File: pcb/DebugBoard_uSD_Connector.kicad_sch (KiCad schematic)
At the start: 10 parts, among them J5 0472192001

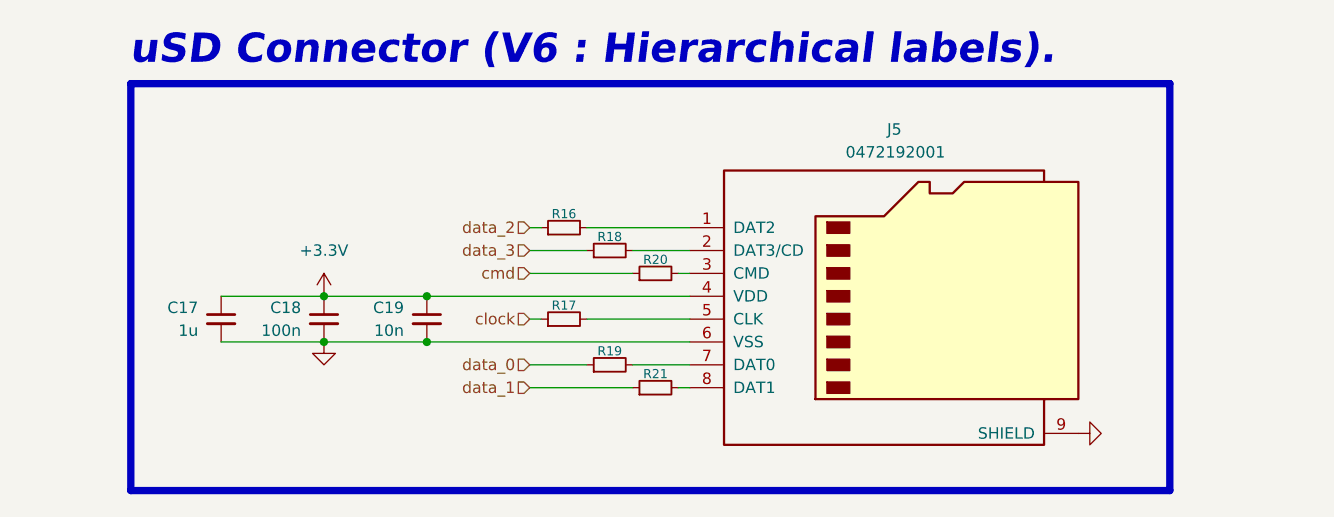
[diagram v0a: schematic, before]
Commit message: Updated uSD connector for `DebugBoard`.
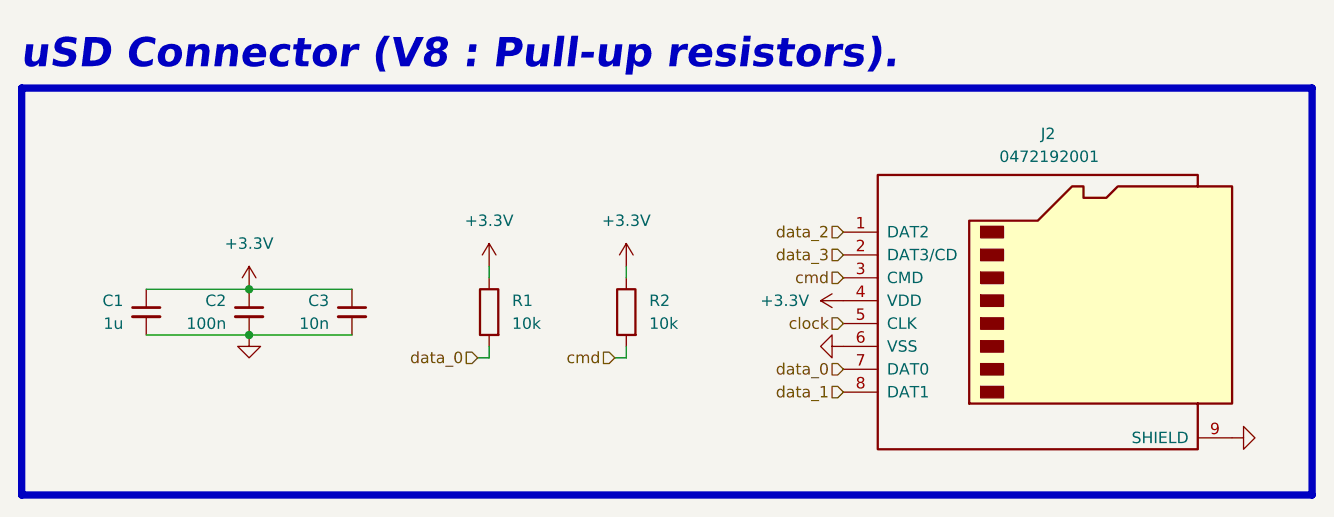
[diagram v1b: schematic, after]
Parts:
- removed R16, R17, R18, R19, R20, R21: R_Small, Resistor_SMD:R_1206_3216Metric_Pad1.30x1.75mm_HandSolder, symbol Device:R_Small
- added R1, R2: 10k, Resistor_SMD:R_1206_3216Metric_Pad1.30x1.75mm_HandSolder, symbol Device:R
- renumbered C17 to C1, C18 to C2, C19 to C3, J5 to J2
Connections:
- net +3.3V: now also R1.1, R2.1
- net clock: now also J2.5 (CLK)
- net cmd: now also J2.3 (CMD), R2.2
- net data_0: now also J2.7 (DAT0), R1.2
- net data_1: now also J2.8 (DAT1)
- net data_2: now also J2.1 (DAT2)
- net data_3: now also J2.2 (DAT3/CD)
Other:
- note added: "uSD Connector (V8 : Pull-up resistors)."
- note removed: "uSD Connector (V6 : Hierarchical labels)."
- moved on the sheet: C1, C2, C3, J2

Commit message: Made `DebugBoard` target and fixed some GPIO discrepancies.
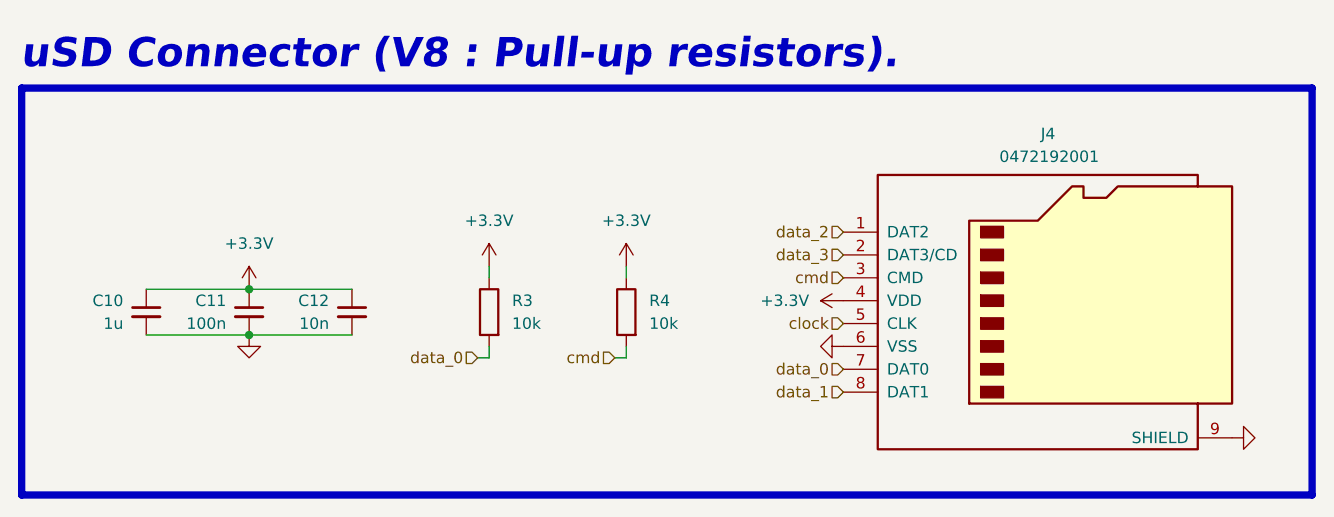
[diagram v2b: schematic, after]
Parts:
- renumbered C1 to C10, C2 to C11, C3 to C12, J2 to J4, R1 to R3, R2 to R4
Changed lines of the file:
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@@
 		(dnp no)
 		(fields_autoplaced yes)
-		(property "Reference" "#PWR?"
+		(property "Reference" "#PWR027"
 			(at 127.5715 77.9627 0)
 			(effects
@@
 			(project ""
 				(path "/5ece3d0a-e9bb-4e6a-946b-805aaca75ace/2e1c1ed4-1bb2-4fa0-a9e0-4cf82a925b94"
-					(reference "#PWR?")
+					(reference "#PWR027")
 					(unit 1)
 				)
@@
 		(dnp no)
 		(fields_autoplaced yes)
-		(property "Reference" "#PWR?"
+		(property "Reference" "#PWR026"
 			(at 99.6315 77.9627 0)
 			(effects
@@
 			(project ""
 				(path "/5ece3d0a-e9bb-4e6a-946b-805aaca75ace/2e1c1ed4-1bb2-4fa0-a9e0-4cf82a925b94"
-					(reference "#PWR?")
+					(reference "#PWR026")
 					(unit 1)
 				)
@@
 		(on_board yes)
 		(dnp no)
-		(property "Reference" "R2"
+		(property "Reference" "R4"
 			(at 102.1715 77.9626 0)
 			(effects
@@
 			(project ""
 				(path "/5ece3d0a-e9bb-4e6a-946b-805aaca75ace/2e1c1ed4-1bb2-4fa0-a9e0-4cf82a925b94"
-					(reference "R2")
+					(reference "R4")
 					(unit 1)
 				)
@@
 		(on_board yes)
 		(dnp no)
-		(property "Reference" "C1"
+		(property "Reference" "C10"
 			(at 43.7515 77.9689 0)
 			(effects
@@
 			(project ""
 				(path "/5ece3d0a-e9bb-4e6a-946b-805aaca75ace/2e1c1ed4-1bb2-4fa0-a9e0-4cf82a925b94"
-					(reference "C1")
+					(reference "C10")
 					(unit 1)
 				)
@@
 		(on_board yes)
 		(dnp no)
-		(property "Reference" "C2"
+		(property "Reference" "C11"
 			(at 55.1815 77.9689 0)
 			(effects
@@
 			(project ""
 				(path "/5ece3d0a-e9bb-4e6a-946b-805aaca75ace/2e1c1ed4-1bb2-4fa0-a9e0-4cf82a925b94"
-					(reference "C2")
+					(reference "C11")
 					(unit 1)
 				)
@@
 		(on_board yes)
 		(dnp no)
-		(property "Reference" "J2"
+		(property "Reference" "J4"
 			(at 146.4945 59.4207 0)
 			(effects
@@
 			(project ""
 				(path "/5ece3d0a-e9bb-4e6a-946b-805aaca75ace/2e1c1ed4-1bb2-4fa0-a9e0-4cf82a925b94"
-					(reference "J2")
+					(reference "J4")
 					(unit 1)
 				)
@@
 		(dnp no)
 		(fields_autoplaced yes)
-		(property "Reference" "#PWR?"
+		(property "Reference" "#PWR024"
 			(at 57.7215 88.1227 0)
 			(effects
@@
 			(project ""
 				(path "/5ece3d0a-e9bb-4e6a-946b-805aaca75ace/2e1c1ed4-1bb2-4fa0-a9e0-4cf82a925b94"
-					(reference "#PWR?")
+					(reference "#PWR024")
 					(unit 1)
 				)
@@
 		(dnp no)
 		(fields_autoplaced yes)
-		(property "Reference" "#PWR?"
+		(property "Reference" "#PWR023"
 			(at 57.7215 80.5027 0)
 			(effects
@@
 			(project ""
 				(path "/5ece3d0a-e9bb-4e6a-946b-805aaca75ace/2e1c1ed4-1bb2-4fa0-a9e0-4cf82a925b94"
-					(reference "#PWR?")
+					(reference "#PWR023")
 					(unit 1)
 				)
@@
 		(dnp no)
 		(fields_autoplaced yes)
-		(property "Reference" "#PWR?"
+		(property "Reference" "#PWR028"
 			(at 117.4115 83.0427 0)
 			(effects
@@
 			(project ""
 				(path "/5ece3d0a-e9bb-4e6a-946b-805aaca75ace/2e1c1ed4-1bb2-4fa0-a9e0-4cf82a925b94"
-					(reference "#PWR?")
+					(reference "#PWR028")
 					(unit 1)
 				)
@@
 		(dnp no)
 		(fields_autoplaced yes)
-		(property "Reference" "#PWR?"
+		(property "Reference" "#PWR025"
 			(at 84.3915 77.9627 0)
 			(effects
@@
 			(project ""
 				(path "/5ece3d0a-e9bb-4e6a-946b-805aaca75ace/2e1c1ed4-1bb2-4fa0-a9e0-4cf82a925b94"
-					(reference "#PWR?")
+					(reference "#PWR025")
 					(unit 1)
 				)
@@
 		(dnp no)
 		(fields_autoplaced yes)
-		(property "Reference" "#PWR?"
+		(property "Reference" "#PWR029"
 			(at 173.2915 93.2027 0)
 			(effects
@@
 			(project ""
 				(path "/5ece3d0a-e9bb-4e6a-946b-805aaca75ace/2e1c1ed4-1bb2-4fa0-a9e0-4cf82a925b94"
-					(reference "#PWR?")
+					(reference "#PWR029")
 					(unit 1)
 				)
@@
 		(on_board yes)
 		(dnp no)
-		(property "Reference" "R1"
+		(property "Reference" "R3"
 			(at 86.9315 77.9626 0)
 			(effects
@@
 			(project ""
 				(path "/5ece3d0a-e9bb-4e6a-946b-805aaca75ace/2e1c1ed4-1bb2-4fa0-a9e0-4cf82a925b94"
-					(reference "R1")
+					(reference "R3")
 					(unit 1)
 				)
@@
 		(on_board yes)
 		(dnp no)
-		(property "Reference" "C3"
+		(property "Reference" "C12"
 			(at 66.6115 77.9689 0)
 			(effects
@@
 			(project ""
 				(path "/5ece3d0a-e9bb-4e6a-946b-805aaca75ace/2e1c1ed4-1bb2-4fa0-a9e0-4cf82a925b94"
-					(reference "C3")
-					(unit 1)
-				)
+					(reference "C12")
+					(unit 1)
+				)

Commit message: Laid out and routed `DebugBoard`.
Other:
- moved on the sheet: C10, C11, C12, J4, R3, R4

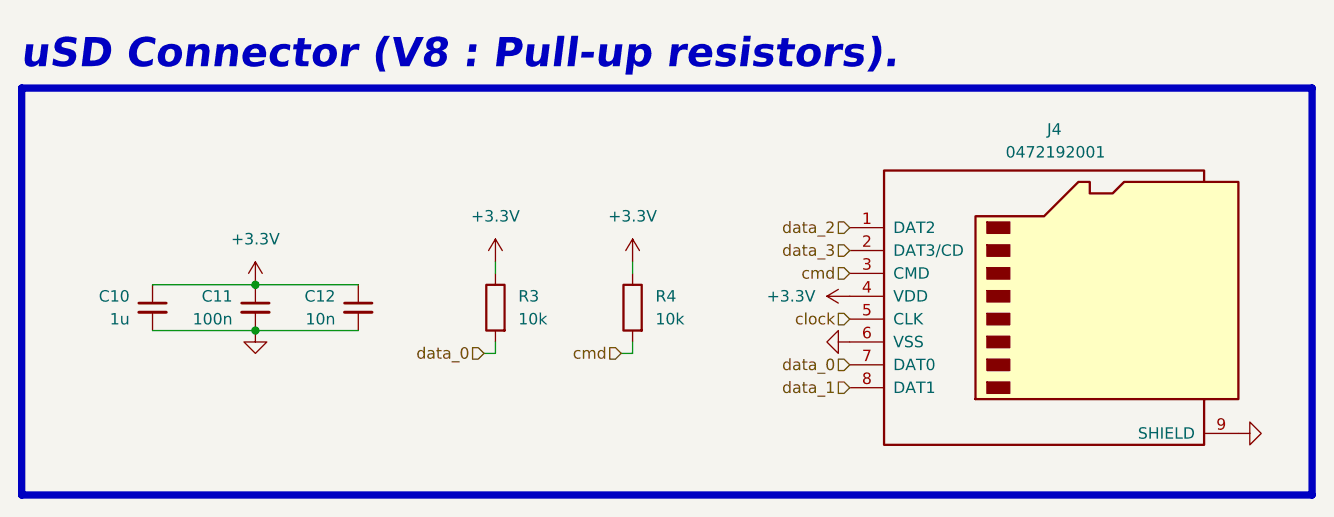
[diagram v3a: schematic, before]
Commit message: Placed silkscreen for `DebugBoard`.
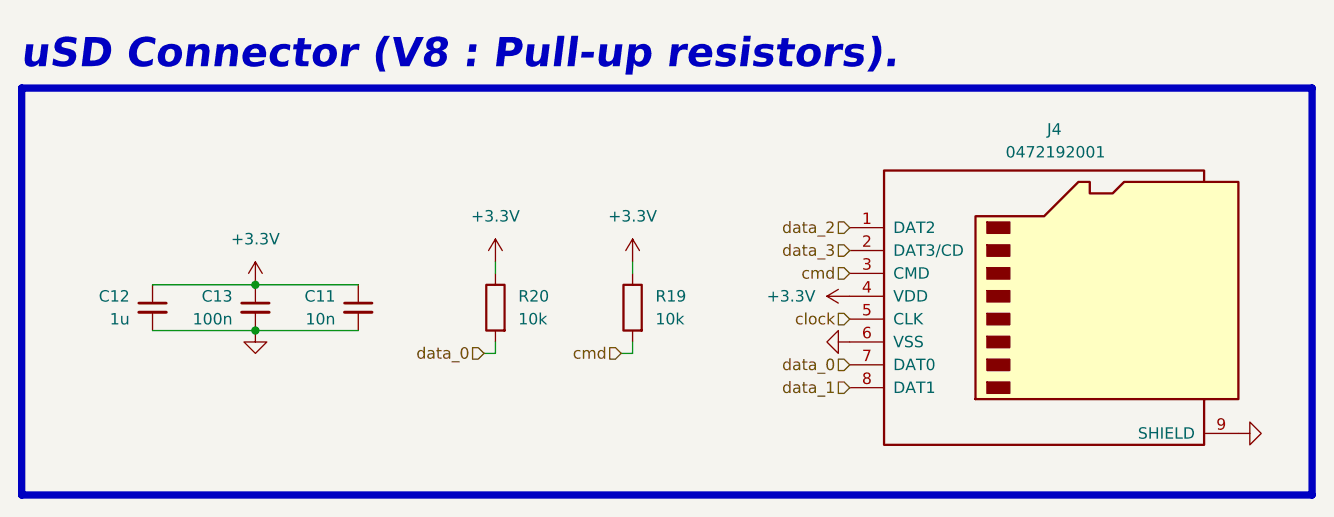
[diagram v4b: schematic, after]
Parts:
- renumbered C12 to C11, C10 to C12, C11 to C13, R4 to R19, R3 to R20
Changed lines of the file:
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@@
 		(on_board yes)
 		(dnp no)
-		(property "Reference" "R4"
+		(property "Reference" "R19"
 			(at 102.87 77.4699 0)
 			(effects
@@
 			(project ""
 				(path "/5ece3d0a-e9bb-4e6a-946b-805aaca75ace/2e1c1ed4-1bb2-4fa0-a9e0-4cf82a925b94"
-					(reference "R4")
+					(reference "R19")
 					(unit 1)
 				)
@@
 		(on_board yes)
 		(dnp no)
-		(property "Reference" "C10"
+		(property "Reference" "C12"
 			(at 44.45 77.4762 0)
 			(effects
@@
 			(project ""
 				(path "/5ece3d0a-e9bb-4e6a-946b-805aaca75ace/2e1c1ed4-1bb2-4fa0-a9e0-4cf82a925b94"
-					(reference "C10")
+					(reference "C12")
 					(unit 1)
 				)
@@
 		(on_board yes)
 		(dnp no)
-		(property "Reference" "C11"
+		(property "Reference" "C13"
 			(at 55.88 77.4762 0)
 			(effects
@@
 			(project ""
 				(path "/5ece3d0a-e9bb-4e6a-946b-805aaca75ace/2e1c1ed4-1bb2-4fa0-a9e0-4cf82a925b94"
-					(reference "C11")
+					(reference "C13")
 					(unit 1)
 				)
@@
 		(on_board yes)
 		(dnp no)
-		(property "Reference" "R3"
+		(property "Reference" "R20"
 			(at 87.63 77.4699 0)
 			(effects
@@
 			(project ""
 				(path "/5ece3d0a-e9bb-4e6a-946b-805aaca75ace/2e1c1ed4-1bb2-4fa0-a9e0-4cf82a925b94"
-					(reference "R3")
+					(reference "R20")
 					(unit 1)
 				)
@@
 		(on_board yes)
 		(dnp no)
-		(property "Reference" "C12"
+		(property "Reference" "C11"
 			(at 67.31 77.4762 0)
 			(effects
@@
 			(project ""
 				(path "/5ece3d0a-e9bb-4e6a-946b-805aaca75ace/2e1c1ed4-1bb2-4fa0-a9e0-4cf82a925b94"
-					(reference "C12")
-					(unit 1)
-				)
+					(reference "C11")
+					(unit 1)
+				)
